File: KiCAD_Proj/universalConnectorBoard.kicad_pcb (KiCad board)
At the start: 2 copper layers, 3 parts, among them U1 SC0915_PicoDevModule, U2 TMC2209_MotorDriver, U3 TMC2209_MotorDriver

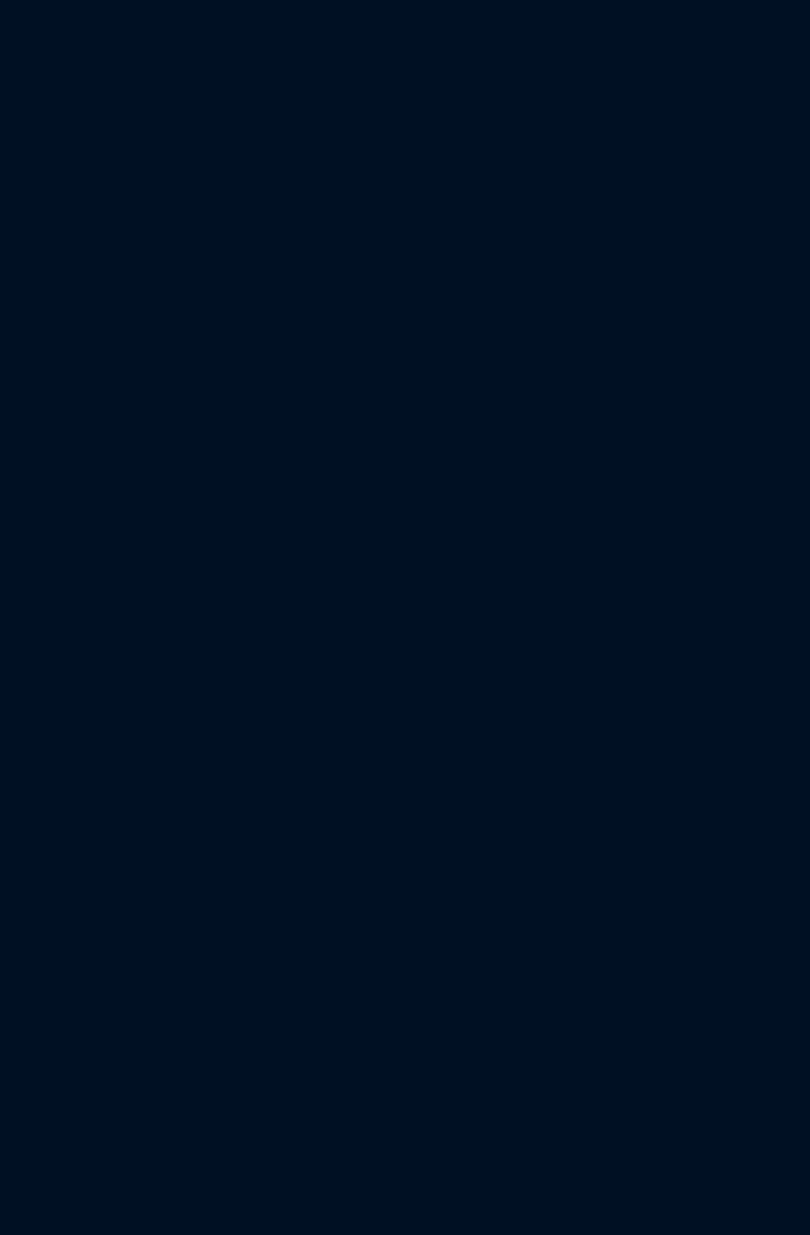
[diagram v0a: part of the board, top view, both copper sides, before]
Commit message: Add pico board footprint with through-hole and smd in one, just found it and thought it is something for the PCB.
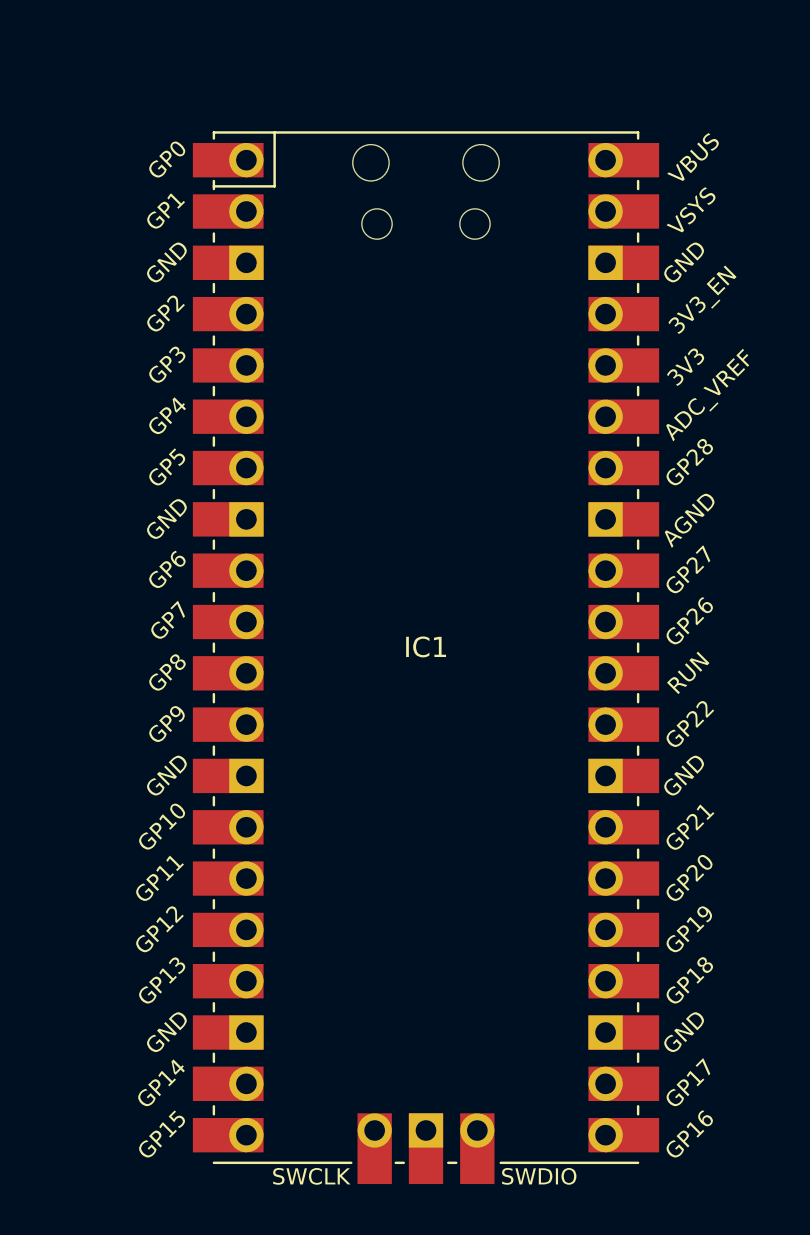
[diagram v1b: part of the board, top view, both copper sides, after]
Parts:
- added IC1: RPI_Pico_EvaluationBoard, Healthbot-Footprints:RPi_Pico_SMD_TH, F.Cu at (163.8, 69.8)

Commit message: Multiple additions
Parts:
- removed U1: SC0915_PicoDevModule, SC0915:MODULE_SC0915
- added C1: 0.10μF, Capacitor_SMD:C_0603_1608Metric_Pad1.08x0.95mm_HandSolder, F.Cu at (141.4, 58.4)
- added C2: C, Capacitor_SMD:C_0603_1608Metric_Pad1.08x0.95mm_HandSolder, F.Cu at (207.4, 83.8)
- added C3: C, Capacitor_SMD:C_0603_1608Metric_Pad1.08x0.95mm_HandSolder, F.Cu at (207.4, 86.4)
- added IC2: SN74LV4052ADR, Healthbot-Footprints:SOIC127P600X175-16N, F.Cu at (144.4, 76.2)
- added J1: 691401700003B, SamacSys_Parts:691401700003B, F.Cu at (193.2, 38.1)
- added J2: Display1, Connector_JST:JST_XH_S7B-XH-A_1x07_P2.50mm_Horizontal, F.Cu at (182.1, 95.6)
- added J3: Display2, Connector_JST:JST_XH_S7B-XH-A_1x07_P2.50mm_Horizontal, F.Cu at (189.6, 88.8)
- added J4: GPIO, Connector_PinHeader_2.54mm:PinHeader_2x20_P2.54mm_Vertical_SMD, F.Cu at (109.2, 76.2)
- added J5: Ledstrip2, Connector_JST:JST_XH_S3B-XH-A_1x03_P2.50mm_Horizontal, F.Cu at (147.7, 100.3)
- added J6: MUX3_UART, Connector_PinSocket_2.54mm:PinSocket_1x04_P2.54mm_Vertical, F.Cu at (121.9, 86.4)
- added J7: MUX4_UART, Connector_PinSocket_2.54mm:PinSocket_1x04_P2.54mm_Vertical, F.Cu at (121.9, 99.1)
- added J8: Ledstrip1, Connector_JST:JST_XH_S4B-XH-A_1x04_P2.50mm_Horizontal, F.Cu at (133.3, 100.3)
- added R1: 100k, Resistor_SMD:R_0603_1608Metric_Pad0.98x0.95mm_HandSolder, F.Cu at (138.5, 84.8)
- added R10: 470, Resistor_SMD:R_0603_1608Metric_Pad0.98x0.95mm_HandSolder, F.Cu at (148.9, 94.0)
- added R2: 100k, Resistor_SMD:R_0603_1608Metric_Pad0.98x0.95mm_HandSolder, F.Cu at (138.5, 82.2)
- added R3: 100k, Resistor_SMD:R_0603_1608Metric_Pad0.98x0.95mm_HandSolder, F.Cu at (138.5, 79.7)
- added R4: 100k, Resistor_SMD:R_0603_1608Metric_Pad0.98x0.95mm_HandSolder, F.Cu at (138.5, 77.2)
- added R5: 100k, Resistor_SMD:R_0603_1608Metric_Pad0.98x0.95mm_HandSolder, F.Cu at (138.5, 74.7)
- added R6: 100k, Resistor_SMD:R_0603_1608Metric_Pad0.98x0.95mm_HandSolder, F.Cu at (138.5, 72.2)
- added R7: 100k, Resistor_SMD:R_0603_1608Metric_Pad0.98x0.95mm_HandSolder, F.Cu at (138.5, 69.7)
- added R8: 100k, Resistor_SMD:R_0603_1608Metric_Pad0.98x0.95mm_HandSolder, F.Cu at (138.5, 67.2)
- added R9: 470, Resistor_SMD:R_0603_1608Metric_Pad0.98x0.95mm_HandSolder, F.Cu at (138.8, 94.0)
- added U2: LM1117DT-3.3, Package_TO_SOT_SMD:TO-252-3_TabPin2, F.Cu at (200.7, 48.3)
- moved U3 34.3 mm to (128.3, 50.8)
- moved U4 34.3 mm to (128.3, 73.7)
- renumbered U2 to U3, U3 to U4
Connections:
- IC1 pad 1: unconnected-(IC1-GPIO0-Pad1) -> /TX_PICO
- IC1 pad 11: unconnected-(IC1-GPIO8-Pad11) -> /Display_DC
- IC1 pad 12: unconnected-(IC1-GPIO9-Pad12) -> /Display1_CS
- IC1 pad 13: unconnected-(IC1-GND-Pad13) -> GND
- IC1 pad 14: unconnected-(IC1-GPIO10-Pad14) -> /Display_SDA
- IC1 pad 15: unconnected-(IC1-GPIO11-Pad15) -> /Display_SCL
- IC1 pad 16: unconnected-(IC1-GPIO12-Pad16) -> /Display_RES
- IC1 pad 17: unconnected-(IC1-GPIO13-Pad17) -> /Display2_CS
- IC1 pad 18: unconnected-(IC1-GND-Pad18) -> GND
- IC1 pad 2: unconnected-(IC1-GPIO1-Pad2) -> /RX_PICO
- IC1 pad 23: unconnected-(IC1-GND-Pad23) -> GND
- IC1 pad 28: unconnected-(IC1-GND-Pad28) -> GND
- IC1 pad 3: unconnected-(IC1-GND-Pad3) -> GND
- IC1 pad 38: unconnected-(IC1-GND-Pad38) -> GND
- IC1 pad 4: unconnected-(IC1-GPIO2-Pad4) -> /A
- IC1 pad 42: unconnected-(IC1-GND-Pad42) -> GND
- IC1 pad 5: unconnected-(IC1-GPIO3-Pad5) -> /B
- IC1 pad 6: unconnected-(IC1-GPIO4-Pad6) -> /INH
- IC1 pad 7: unconnected-(IC1-GPIO5-Pad7) -> /Ledstrip1_DATA
- IC1 pad 8: unconnected-(IC1-GND-Pad8) -> GND
- IC1 pad 9: unconnected-(IC1-GPIO6-Pad9) -> /Ledstrip2_DATA
- U3 pad 10: Net-(U1-GP1) -> unconnected-(U3-STEP-Pad10)
- U3 pad 12: unconnected-(U2-RX-Pad12) -> /MUX_TX1
- U3 pad 13: unconnected-(U2-TX-Pad13) -> /MUX_RX1
- U3 pad 16: Net-(U1-GP2) -> unconnected-(U3-~{EN}-Pad16)
- U3 pad 9: Net-(U1-GP0) -> unconnected-(U3-DIR-Pad9)
- U4 pad 10: Net-(U1-GP4) -> unconnected-(U4-STEP-Pad10)
- U4 pad 12: unconnected-(U3-RX-Pad12) -> /MUX_TX2
- U4 pad 13: unconnected-(U3-TX-Pad13) -> /MUX_RX2
- U4 pad 16: Net-(U1-GP5) -> unconnected-(U4-~{EN}-Pad16)
- U4 pad 9: Net-(U1-GP3) -> unconnected-(U4-DIR-Pad9)

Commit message: Added lots of connections
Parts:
- added JP2: Jumper_3_Bridged12, Connector_PinHeader_2.54mm:PinHeader_1x03_P2.54mm_Vertical, F.Cu at (143.5, 35.6)
- C2, C3: value C -> 1000μF
- J4: value GPIO -> RPI4
- moved C1 22.7 mm to (151.5, 38.1)
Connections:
- C1 pad 1: VCC -> Net-(IC2-VCC)
- C1 pad 2: Net-(IC2-VCC) -> GND
- IC1 pad 1: /TX_PICO -> /RXD_PI4
- IC1 pad 10: unconnected-(IC1-GPIO7-Pad10) -> /Leds_Cheeks
- IC1 pad 2: /RX_PICO -> /TXD_PI4
- IC1 pad 21: unconnected-(IC1-GPIO16-Pad21) -> /TX_PICO
- IC1 pad 22: unconnected-(IC1-GPIO17-Pad22) -> /RX_PICO
- J4 pad 10: unconnected-(J4-Pin_10-Pad10) -> /RXD_PI4
- J4 pad 8: unconnected-(J4-Pin_8-Pad8) -> /TXD_PI4
- U3 pad 10: unconnected-(U3-STEP-Pad10) -> /MD1_STEP
- U3 pad 16: unconnected-(U3-~{EN}-Pad16) -> /MD1_EN
- U3 pad 9: unconnected-(U3-DIR-Pad9) -> /MD1_DIR
- U4 pad 10: unconnected-(U4-STEP-Pad10) -> /MD2_STEP
- U4 pad 16: unconnected-(U4-~{EN}-Pad16) -> /MD2_EN
- U4 pad 9: unconnected-(U4-DIR-Pad9) -> /MD3_STEP

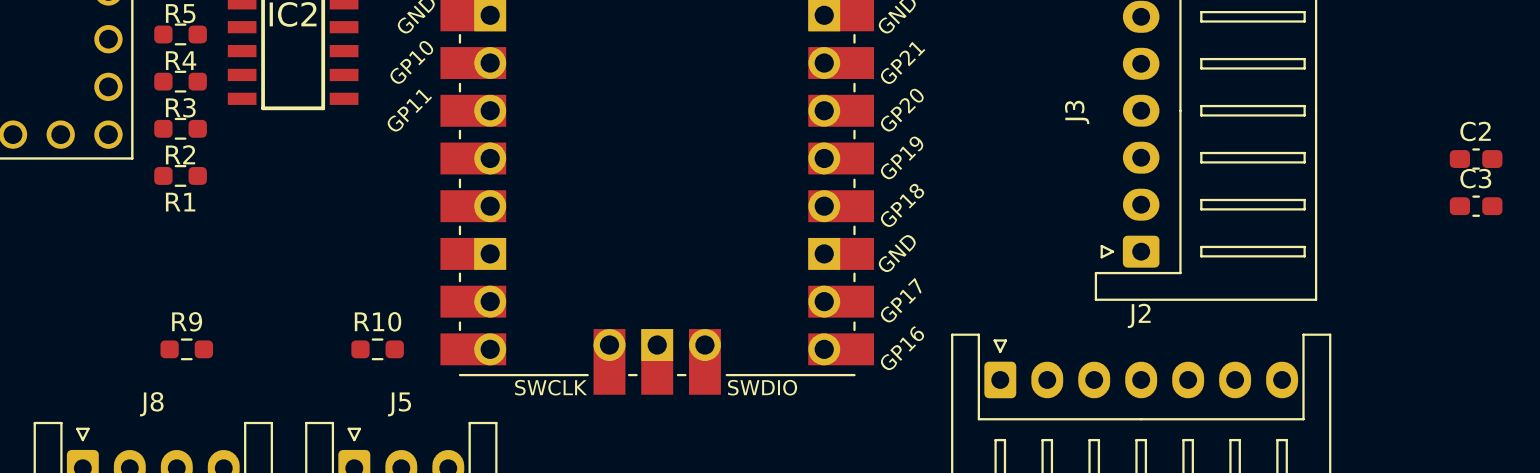
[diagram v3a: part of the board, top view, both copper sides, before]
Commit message: All pico GPIO pins assigned
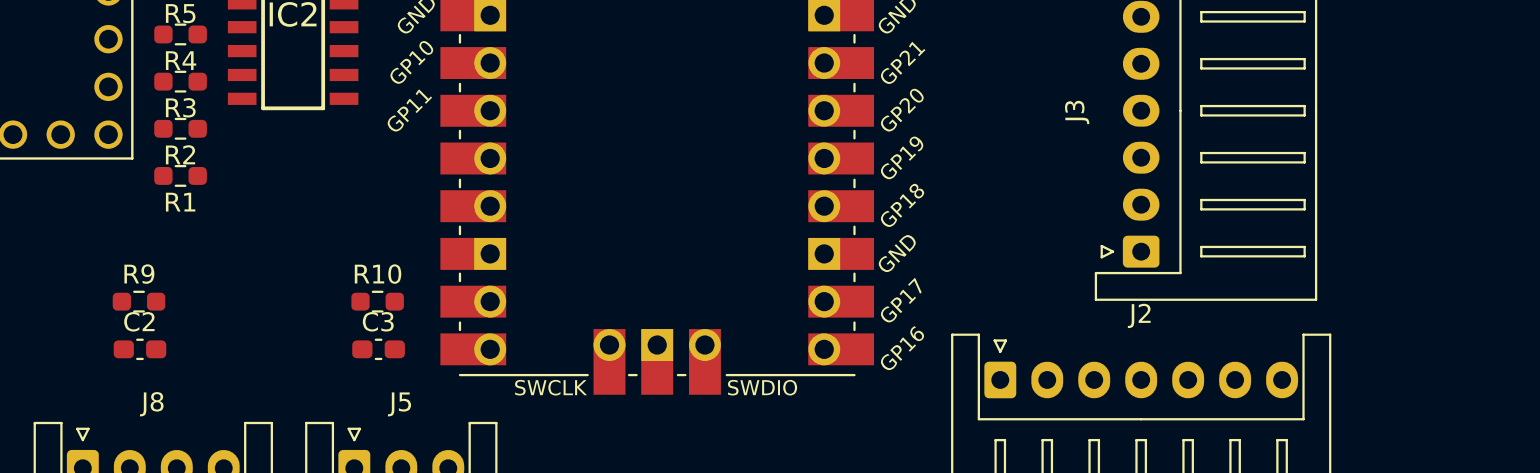
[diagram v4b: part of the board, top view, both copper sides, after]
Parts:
- moved C2 71.8 mm to (136.3, 94.0)
- moved C3 58.9 mm to (149.0, 94.0)
- moved R9 3.59 mm to (136.2, 91.4)
- moved R10 2.54 mm to (148.9, 91.4)
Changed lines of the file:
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@@
   )
   (footprint "Resistor_SMD:R_0603_1608Metric_Pad0.98x0.95mm_HandSolder" (layer "F.Cu")
-    (at 138.7875 93.98)
+    (at 136.2475 91.44)
     (descr "Resistor SMD 0603 (1608 Metric), square (rectangular) end terminal, IPC_7351 nominal with elongated pad for handsoldering. (Body size source: IPC-SM-782 page 72, https://www.pcb-3d.com/wordpress/wp-content/uploads/ipc-sm-782a_amendment_1_and_2.pdf), generated with kicad-footprint-generator")
     (tags "resistor handsolder")
@@
   )
   (footprint "Resistor_SMD:R_0603_1608Metric_Pad0.98x0.95mm_HandSolder" (layer "F.Cu")
-    (at 148.9475 93.98)
+    (at 148.9475 91.44)
     (descr "Resistor SMD 0603 (1608 Metric), square (rectangular) end terminal, IPC_7351 nominal with elongated pad for handsoldering. (Body size source: IPC-SM-782 page 72, https://www.pcb-3d.com/wordpress/wp-content/uploads/ipc-sm-782a_amendment_1_and_2.pdf), generated with kicad-footprint-generator")
     (tags "resistor handsolder")
@@
   )
   (footprint "Capacitor_SMD:C_0603_1608Metric_Pad1.08x0.95mm_HandSolder" (layer "F.Cu")
-    (at 207.4175 86.36)
+    (at 148.9975 93.98)
     (descr "Capacitor SMD 0603 (1608 Metric), square (rectangular) end terminal, IPC_7351 nominal with elongated pad for handsoldering. (Body size source: IPC-SM-782 page 76, https://www.pcb-3d.com/wordpress/wp-content/uploads/ipc-sm-782a_amendment_1_and_2.pdf), generated with kicad-footprint-generator")
     (tags "capacitor handsolder")
@@
   )
   (footprint "Capacitor_SMD:C_0603_1608Metric_Pad1.08x0.95mm_HandSolder" (layer "F.Cu")
-    (at 207.4175 83.85)
+    (at 136.2975 93.98)
     (descr "Capacitor SMD 0603 (1608 Metric), square (rectangular) end terminal, IPC_7351 nominal with elongated pad for handsoldering. (Body size source: IPC-SM-782 page 76, https://www.pcb-3d.com/wordpress/wp-content/uploads/ipc-sm-782a_amendment_1_and_2.pdf), generated with kicad-footprint-generator")
     (tags "capacitor handsolder")

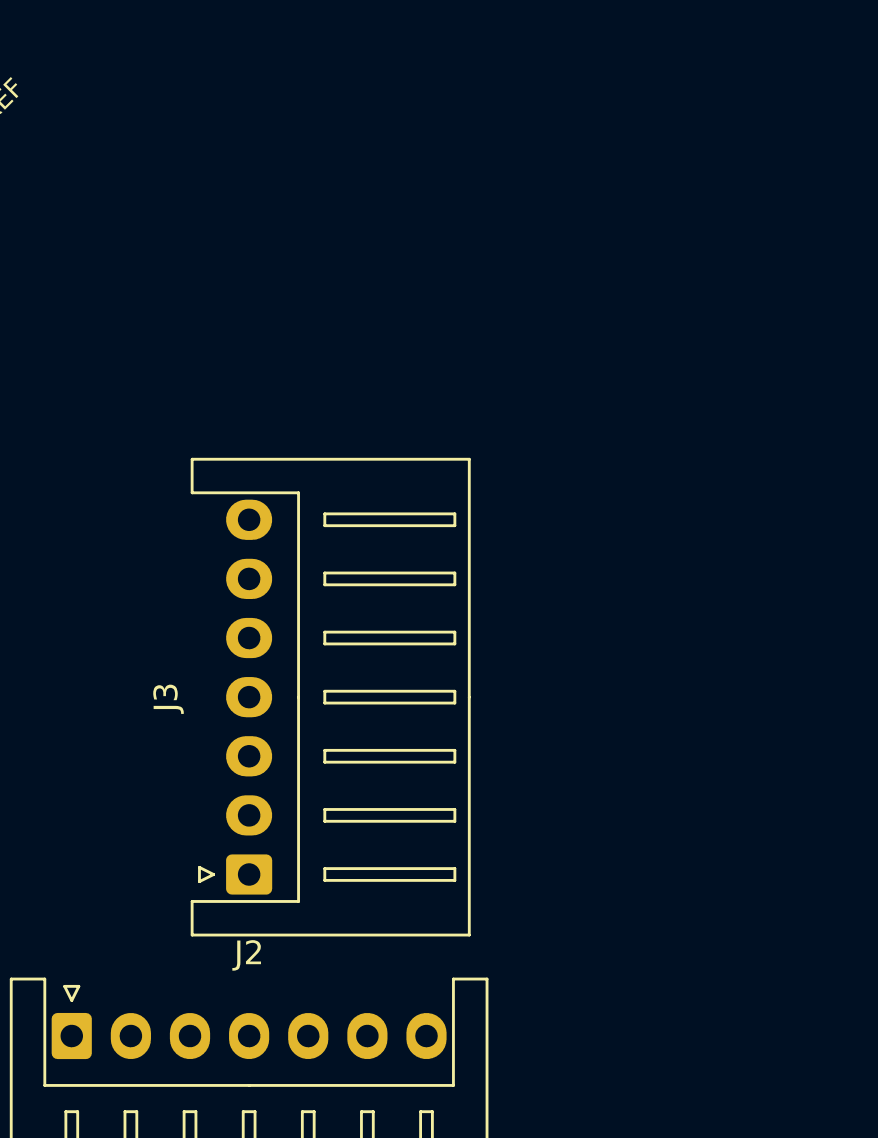
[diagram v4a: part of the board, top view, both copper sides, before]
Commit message: Added excel sheet for overview of pin connections
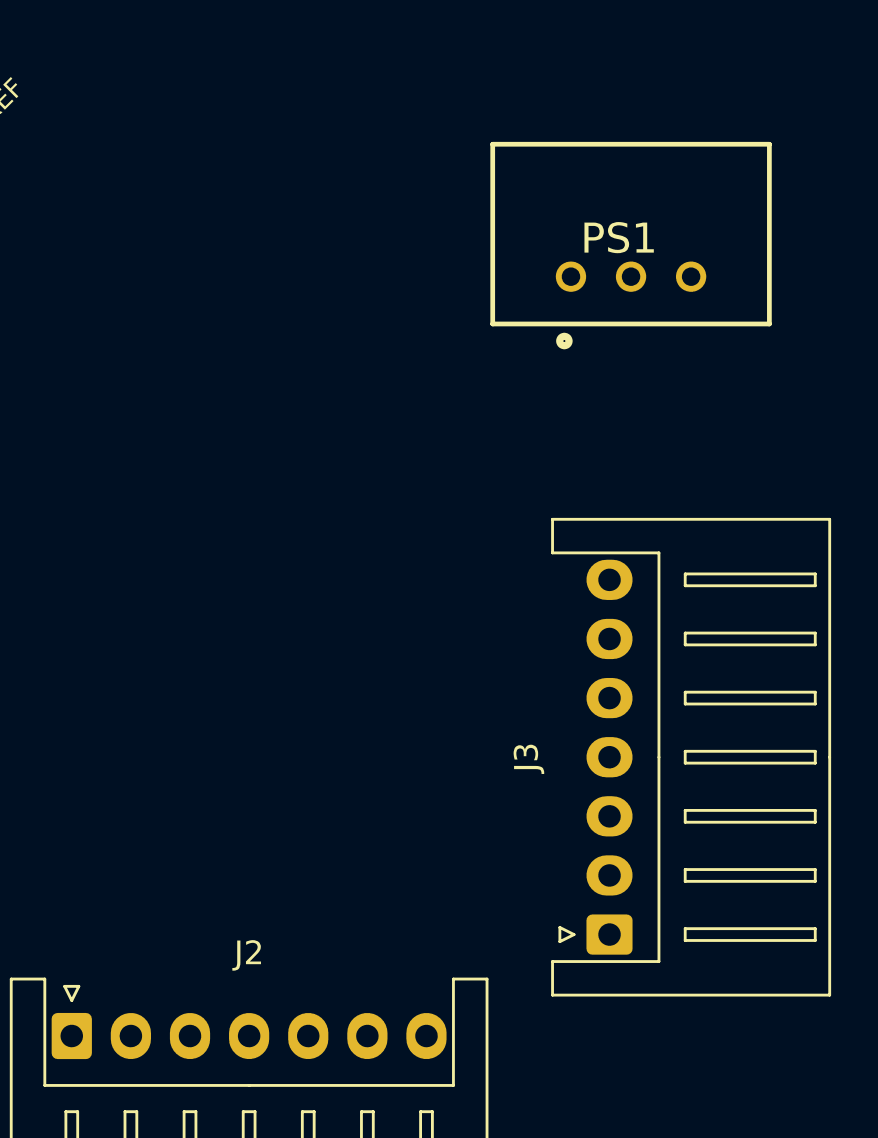
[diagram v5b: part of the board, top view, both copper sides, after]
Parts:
- added PS1: TSR_1-2433, SamacSys_Parts:TSR-1-2433, F.Cu at (205.7, 63.5)
- moved J3 15.5 mm to (204.8, 91.3)
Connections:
- net /MD3_STEP renamed /MD2_DIR
- IC1 pad 10: /Leds_Cheeks -> /MUX_B
- IC1 pad 11: /Display_DC -> /Display_RES
- IC1 pad 14: /Display_SDA -> /Display_DC
- IC1 pad 15: /Display_SCL -> /Display_SDA
- IC1 pad 16: /Display_RES -> /Display_SCL
- IC1 pad 19: unconnected-(IC1-GPIO14-Pad19) -> /MUX_INH
- IC1 pad 20: unconnected-(IC1-GPIO15-Pad20) -> /Ledstrip1_DATA
- IC1 pad 21: /TX_PICO -> /Ledstrip2_DATA
- IC1 pad 22: /RX_PICO -> unconnected-(IC1-GPIO17-Pad22)
- IC1 pad 4: /A -> /LED_Cheeks
- IC1 pad 5: /B -> /LED_Mouth
- IC1 pad 6: /INH -> /TX_PICO
- IC1 pad 7: /Ledstrip1_DATA -> /RX_PICO
- IC1 pad 9: /Ledstrip2_DATA -> /MUX_A
- IC2 pad 10: /A -> /MUX_A
- IC2 pad 6: /INH -> /MUX_INH
- IC2 pad 9: /B -> /MUX_B
- J2 pad 1: /Display1_CS -> /Display_RES
- J2 pad 2: /Display_DC -> /Display1_CS
- J2 pad 3: /Display_SDA -> /Display_DC
- J2 pad 4: /Display_SCL -> /Display_SDA
- J2 pad 5: /Display_RES -> /Display_SCL
- J2 pad 6: +3V3 -> GND
- J2 pad 7: GND -> +3.3V
- J3 pad 1: /Display2_CS -> /Display_RES
- J3 pad 2: /Display_DC -> /Display2_CS
- J3 pad 3: /Display_SDA -> /Display_DC
- J3 pad 4: /Display_SCL -> /Display_SDA
- J3 pad 5: /Display_RES -> /Display_SCL
- J3 pad 6: +3V3 -> GND
- J3 pad 7: GND -> +3.3V
